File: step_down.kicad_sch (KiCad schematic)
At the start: 11 parts, among them IC6 TPS566247DRLR

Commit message: New template
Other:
- company: (none) -> STAPsystem
- title: (none) -> RPM meter LED
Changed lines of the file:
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@@
 	(generator_version "8.0")
 	(paper "A4")
+	(title_block
+		(title "RPM meter LED")
+		(date "2024-11-26")
+		(rev "v1.0")
+		(company "STAPsystem")
+	)
 	(junction
 		(at 88.9 58.42)

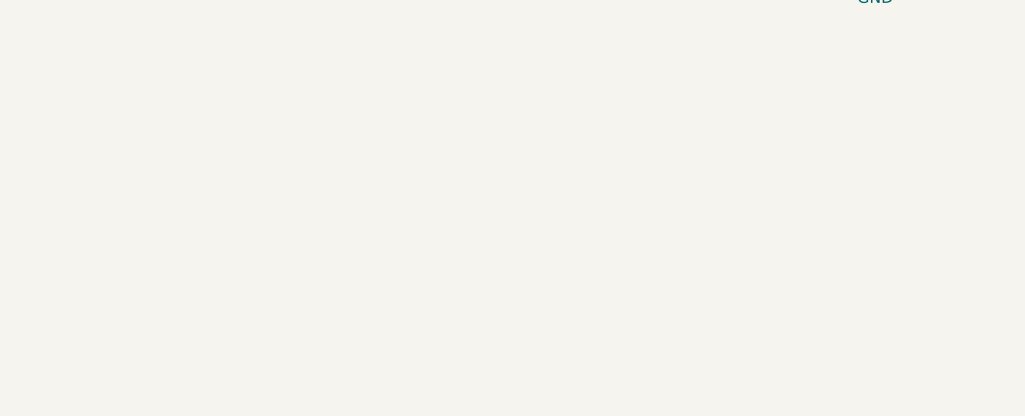
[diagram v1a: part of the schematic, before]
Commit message: LDO 3v3
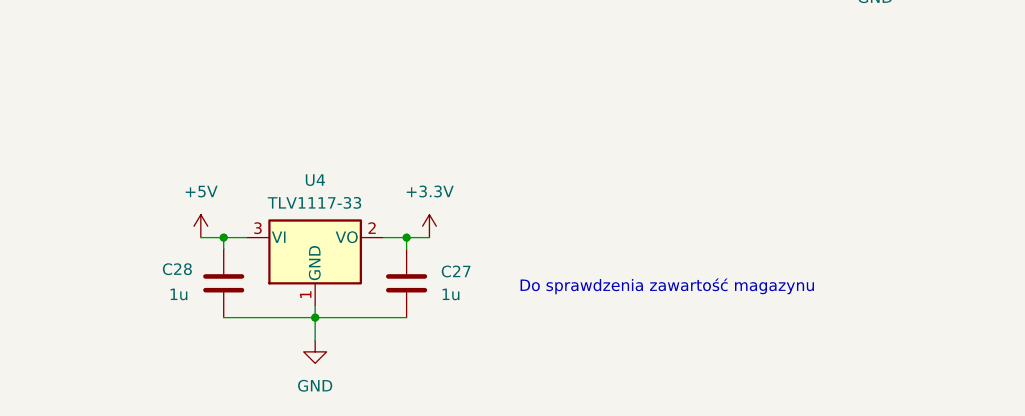
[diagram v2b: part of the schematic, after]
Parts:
- added C27, C28: 1u, Capacitor_SMD:C_0603_1608Metric, symbol Device:C
- added U4: TLV1117-33, Package_TO_SOT_SMD:SOT-223-3_TabPin2, symbol Regulator_Linear:TLV1117-33
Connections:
- net +5V: now also C28.1, U4.3 (VI)
- net GND: now also C27.2, C28.2, U4.1 (GND)
- new net +3.3V: C27.1, U4.2 (VO)
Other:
- note added: "Do sprawdzenia zawartość magazynu"

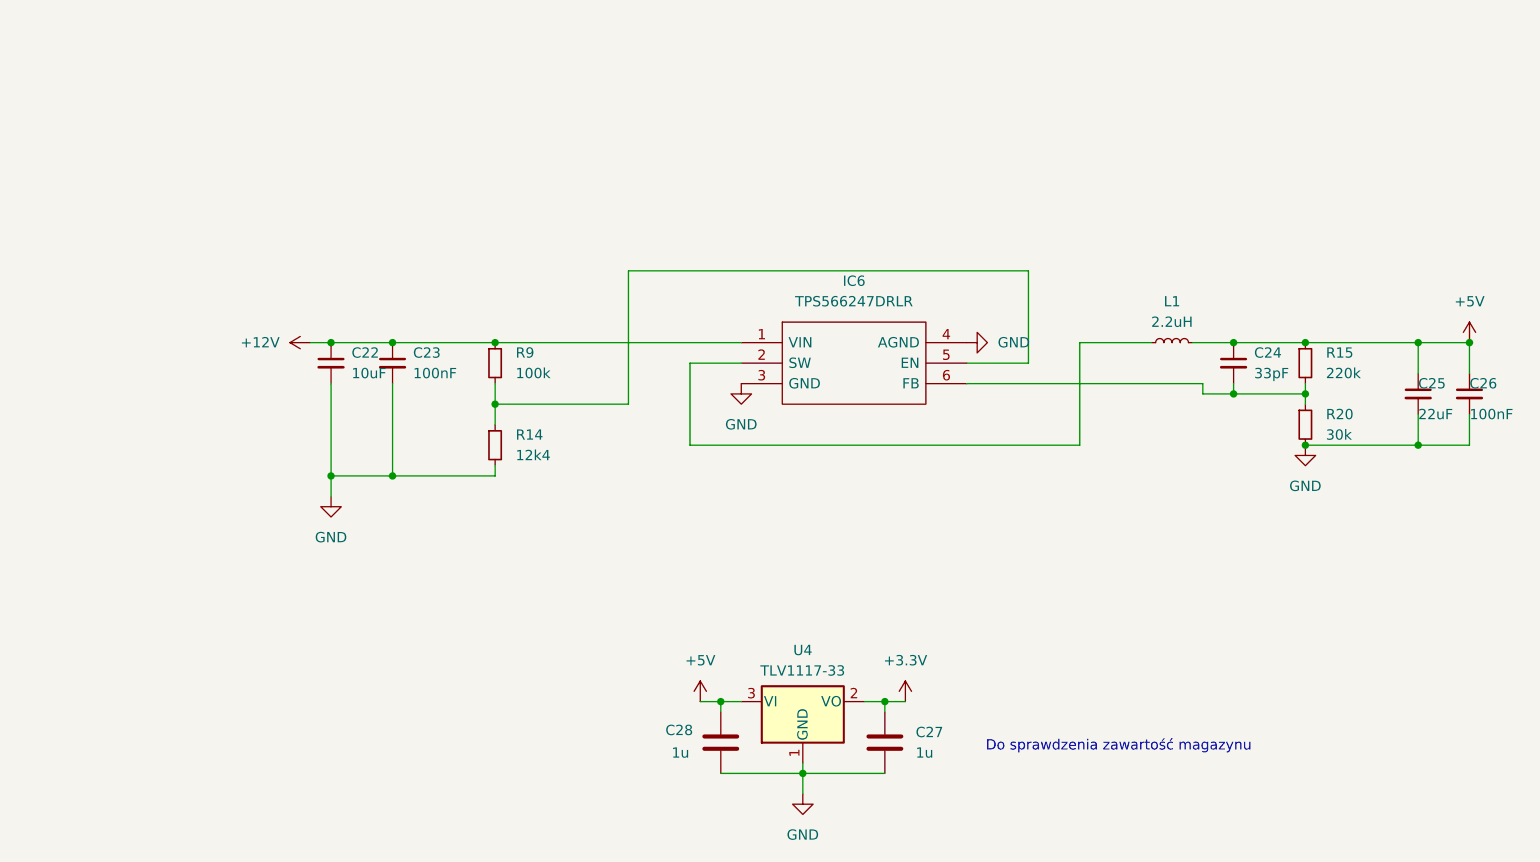
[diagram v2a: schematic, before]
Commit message: TVS protection
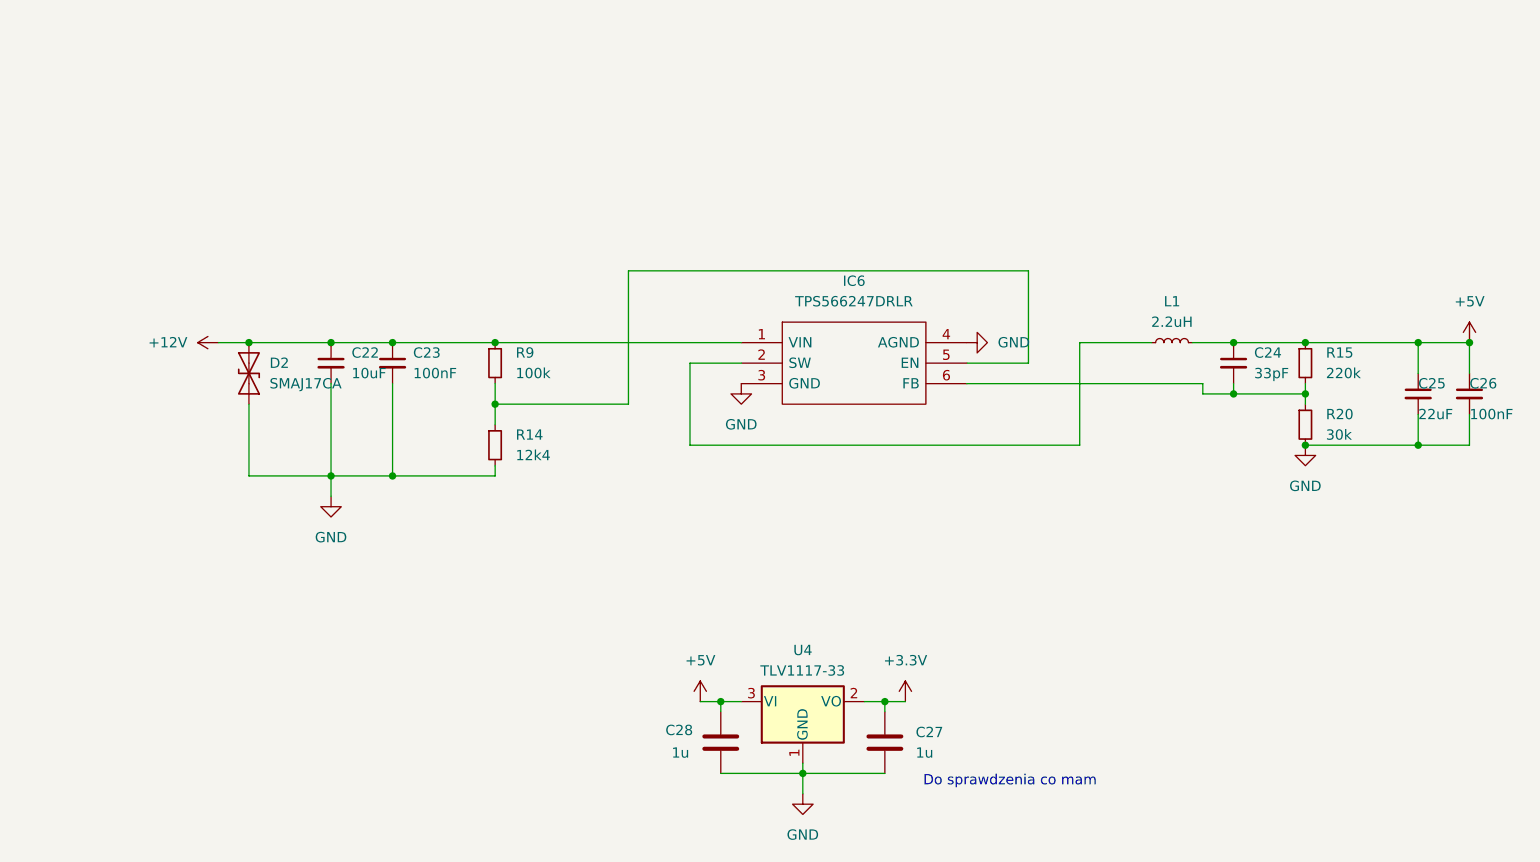
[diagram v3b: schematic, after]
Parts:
- added D2: SMAJ17CA, Diode_SMD:D_SMA, symbol Diode:SMAJ17CA
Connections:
- net +12V: now also D2.2 (A2)
- net GND: now also D2.1 (A1)
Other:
- note added: "Do sprawdzenia co mam"
- note removed: "Do sprawdzenia zawartość magazynu"
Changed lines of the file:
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@@
+	)
+	(junction
+		(at 71.12 58.42)
+		(diameter 0)
+		(color 0 0 0 0)
 	)
 	(junction
@@
 	(wire
 		(pts
+			(xy 71.12 66.04) (xy 71.12 74.93)
+		)
+		(stroke
+			(width 0)
+			(type default)
+		)
+	)
+	(wire
+		(pts
 			(xy 139.7 111.76) (xy 149.86 111.76)
 		)
@@
 	(wire
 		(pts
-			(xy 78.74 58.42) (xy 81.28 58.42)
+			(xy 67.31 58.42) (xy 71.12 58.42)
 		)
 		(stroke
@@
 	(wire
 		(pts
+			(xy 71.12 74.93) (xy 81.28 74.93)
+		)
+		(stroke
+			(width 0)
+			(type default)
+		)
+	)
+	(wire
+		(pts
 			(xy 129.54 102.87) (xy 129.54 104.14)
 		)
@@
 	(wire
 		(pts
+			(xy 71.12 58.42) (xy 81.28 58.42)
+		)
+		(stroke
+			(width 0)
+			(type default)
+		)
+	)
+	(wire
+		(pts
 			(xy 189.23 64.77) (xy 193.04 64.77)
 		)
@@
 		)
 	)
-	(text "Do sprawdzenia zawartość magazynu"
-		(exclude_from_sim no)
-		(at 178.816 108.458 0)
+	(text "Do sprawdzenia co mam"
+		(exclude_from_sim no)
+		(at 165.354 112.776 0)
 		(effects
 			(font
@@
 	)
 	(symbol
+		(lib_id "Diode:SMAJ17CA")
+		(at 71.12 62.23 90)
+		(unit 1)
+		(exclude_from_sim no)
+		(in_bom yes)
+		(on_board yes)
+		(dnp no)
+		(fields_autoplaced yes)
+		(property "Reference" "D2"
+			(at 73.66 60.9599 90)
+			(effects
+				(font
+					(size 1.27 1.27)
+				)
+				(justify right)
+			)
+		)
+		(property "Value" "SMAJ17CA"
+			(at 73.66 63.4999 90)
+			(effects
+				(font
+					(size 1.27 1.27)
+				)
+				(justify right)
+			)
+		)
+		(property "Footprint" "Diode_SMD:D_SMA"
+			(at 76.2 62.23 0)
+			(effects
+				(font
+					(size 1.27 1.27)
+				)
+				(hide yes)
+			)
+		)
+		(property "Datasheet" "https://www.littelfuse.com/media?resourcetype=datasheets&itemid=75e32973-b177-4ee3-a0ff-cedaf1abdb93&filename=smaj-datasheet"
+			(at 71.12 62.23 0)
+			(effects
+				(font
+					(size 1.27 1.27)
+				)
+				(hide yes)
+			)
+		)
+		(property "Description" "400W bidirectional Transient Voltage Suppressor, 17.0Vr, SMA(DO-214AC)"
+			(at 71.12 62.23 0)
+			(effects
+				(font
+					(size 1.27 1.27)
+				)
+				(hide yes)
+			)
+		)
+		(pin "1"
+		)
+		(pin "2"
+		)
+		(instances
+			(project ""
+				(path "/c95b12ac-441d-4f7a-bd6a-c2e5d81eb286/52494463-9471-4829-8fdd-a1729c6b7a2b"
+					(reference "D2")
+					(unit 1)
+				)
+			)
+		)
+	)
+	(symbol
 		(lib_id "Device:R_Small")
 		(at 101.6 60.96 0)
@@
 	(symbol
 		(lib_id "power:+12V")
-		(at 78.74 58.42 90)
+		(at 67.31 58.42 90)
 		(unit 1)
 		(exclude_from_sim no)
@@
 		(fields_autoplaced yes)
 		(property "Reference" "#PWR0112"
-			(at 82.55 58.42 0)
+			(at 71.12 58.42 0)
 			(effects
 				(font
@@
 		)
 		(property "Value" "+12V"
-			(at 74.93 58.4199 90)
+			(at 63.5 58.4199 90)
 			(effects
 				(font
@@
 		)
 		(property "Footprint" ""
-			(at 78.74 58.42 0)
+			(at 67.31 58.42 0)
 			(effects
 				(font
@@
 		)
 		(property "Datasheet" ""
-			(at 78.74 58.42 0)
+			(at 67.31 58.42 0)
 			(effects
 				(font
@@
 		)
 		(property "Description" ""
-			(at 78.74 58.42 0)
-			(effects
-				(font
+			(at 67.31 58.42 0)
+			(effects
+				(font

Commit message: Placed footprints v1.0
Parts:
- added L2: 6,8u, Inductor_SMD:L_6.3x6.3_H3, symbol Device:L
- added R7: 0,1, Resistor_SMD:R_MELF_MMB-0207, symbol Device:R
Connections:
- net +12V: now also R7.1; no longer C22.1, C23.1, D2.2 (A2), IC6.1 (VIN), R9.1
- new net: C22.1, C23.1, D2.2 (A2), L2.1, R7.2
- new net: IC6.1 (VIN), L2.2, R9.1
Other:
- note added: "Do dobrania obudowa"
- note added: "Switching freq: 599.1kHz"
- moved on the sheet: C22, C23, D2

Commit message: New coils footprint
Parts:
- L1: footprint Library_local:XAL5030222MEC -> Library_local:HPI04202R2
- L2: footprint Inductor_SMD:L_6.3x6.3_H3 -> Library_local:HPI06306R8
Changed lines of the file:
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@@
 			)
 		)
-		(property "Footprint" "Inductor_SMD:L_6.3x6.3_H3"
+		(property "Footprint" "Library_local:HPI06306R8"
 			(at 93.98 58.42 0)
 			(effects
@@
 			)
 		)
-		(property "Datasheet" "~"
+		(property "Datasheet" "https://www.tme.eu/pl/details/hpi0630-6r8/dlawiki-smd-mocy/ferrocore/"
 			(at 93.98 58.42 0)
 			(effects
@@
 			)
 		)
-		(property "Footprint" "Library_local:XAL5030222MEC"
+		(property "Footprint" "Library_local:HPI04202R2"
 			(at 185.42 58.42 0)
 			(effects

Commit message: tdk inductions
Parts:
- L1: footprint Library_local:HPI04202R2 -> Library_local:VLCF4020
- L2: footprint Library_local:HPI06306R8 -> Library_local:VLS6045
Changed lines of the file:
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@@
 			)
 		)
-		(property "Footprint" "Library_local:HPI06306R8"
+		(property "Footprint" "Library_local:VLS6045"
 			(at 93.98 58.42 0)
 			(effects
@@
 			)
 		)
-		(property "Datasheet" "https://www.tme.eu/pl/details/hpi0630-6r8/dlawiki-smd-mocy/ferrocore/"
+		(property "Datasheet" "https://www.tme.eu/pl/details/vls6045ex-6r8m/dlawiki-smd-mocy/tdk/"
 			(at 93.98 58.42 0)
 			(effects
@@
 			)
 		)
-		(property "Footprint" "Library_local:HPI04202R2"
+		(property "Footprint" "Library_local:VLCF4020"
 			(at 185.42 58.42 0)
 			(effects
@@
 			)
 		)
-		(property "Datasheet" "~"
+		(property "Datasheet" "https://www.tme.eu/pl/details/vlcf4020t-2r2n1r7/dlawiki-smd-mocy/tdk/"
 			(at 185.42 58.42 0)
 			(effects
